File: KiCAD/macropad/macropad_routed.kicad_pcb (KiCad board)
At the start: 2 copper layers, 114.6 x 122.2 mm, 39 parts

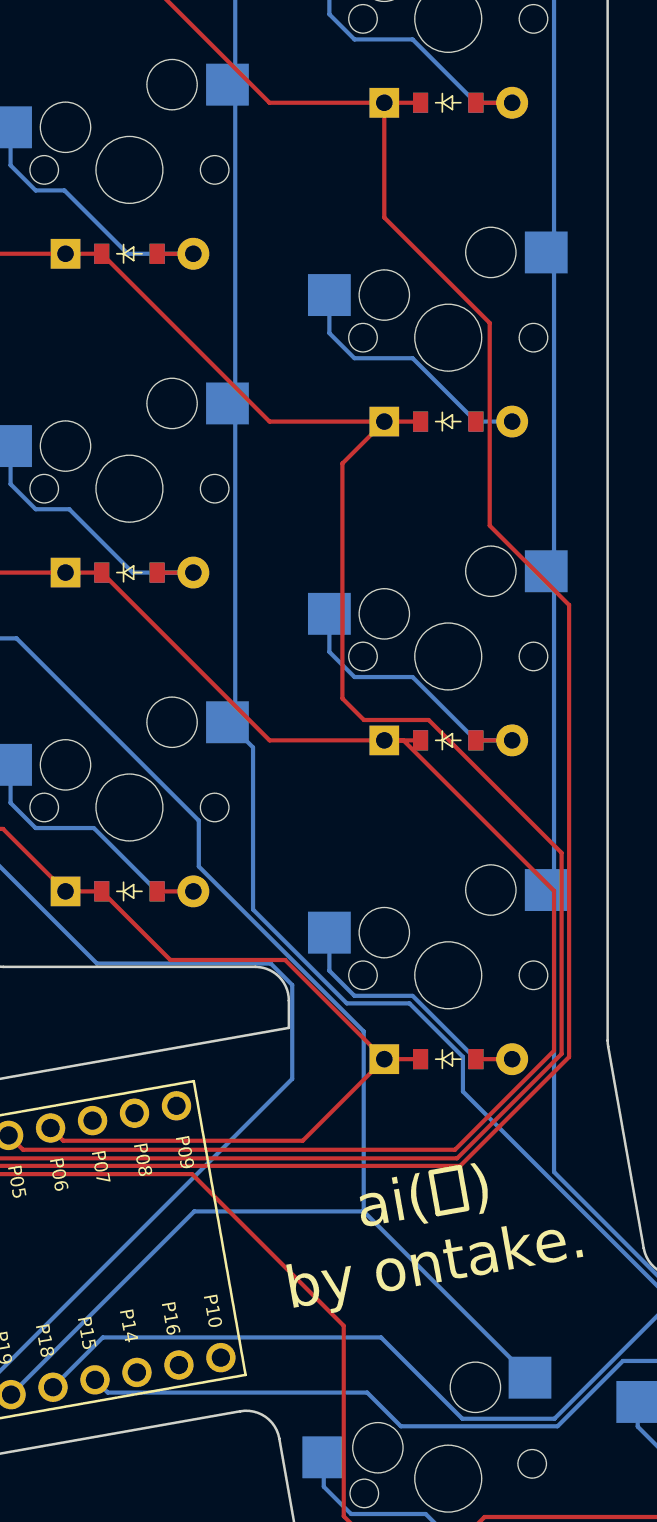
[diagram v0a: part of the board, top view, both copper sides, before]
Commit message: Fix probleme with rounding of the tracks
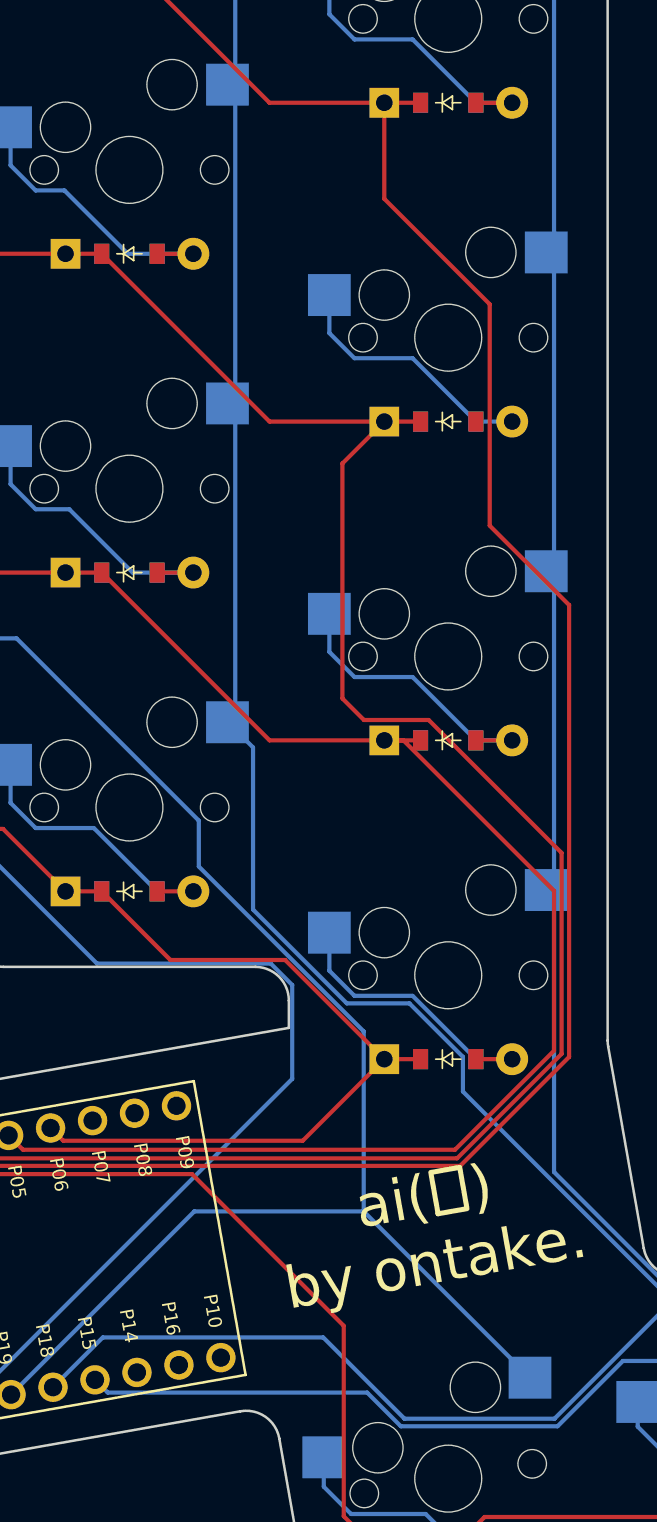
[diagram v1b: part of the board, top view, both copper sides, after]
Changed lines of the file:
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@@
   (segment (start 68.111731 76.886489) (end 64.05325 72.828008) (width 0.25) (layer "B.Cu") (net 8))
   (segment (start 64.05325 72.828008) (end 64.05325 70.56) (width 0.25) (layer "B.Cu") (net 8))
-  (segment (start 130.61 96.222296) (end 130.61 108.300776) (width 0.25) (layer "F.Cu") (net 9))
-  (segment (start 97.867567 146.45952) (end 96.934345 145.526298) (width 0.25) (layer "F.Cu") (net 9))
-  (segment (start 135.342711 139.968724) (end 128.851915 146.45952) (width 0.25) (layer "F.Cu") (net 9))
+  (segment (start 130.61 95.11) (end 130.61 108.300776) (width 0.25) (layer "F.Cu") (net 9))
   (segment (start 80.102829 74.325421) (end 86.32825 68.1) (width 0.25) (layer "F.Cu") (net 9))
   (segment (start 67.32825 78.1) (end 69.48825 78.1) (width 0.25) (layer "F.Cu") (net 9))
@@
   (segment (start 88.48825 68.1) (end 93.48825 73.1) (width 0.25) (layer "F.Cu") (net 9))
   (segment (start 86.32825 68.1) (end 88.48825 68.1) (width 0.25) (layer "F.Cu") (net 9))
-  (segment (start 135.342711 113.033487) (end 135.342711 139.968724) (width 0.25) (layer "F.Cu") (net 9))
   (segment (start 117.48825 83.1) (end 124.32825 83.1) (width 0.25) (layer "F.Cu") (net 9))
   (segment (start 124.32825 83.1) (end 126.48825 83.1) (width 0.25) (layer "F.Cu") (net 9))
   (segment (start 73.262829 74.325421) (end 80.102829 74.325421) (width 0.25) (layer "F.Cu") (net 9))
-  (segment (start 124.32825 89.940546) (end 130.61 96.222296) (width 0.25) (layer "F.Cu") (net 9))
+  (segment (start 135.342711 139.968724) (end 128.851915 146.45952) (width 0.25) (layer "F.Cu") (net 9))
+  (segment (start 97.867567 146.45952) (end 96.934345 145.526298) (width 0.25) (layer "F.Cu") (net 9))
   (segment (start 130.61 108.300776) (end 135.342711 113.033487) (width 0.25) (layer "F.Cu") (net 9))
+  (segment (start 135.342711 113.033487) (end 135.342711 139.968724) (width 0.25) (layer "F.Cu") (net 9))
+  (segment (start 128.851915 146.45952) (end 97.867567 146.45952) (width 0.25) (layer "F.Cu") (net 9))
+  (segment (start 124.32825 83.1) (end 124.32825 88.82825) (width 0.25) (layer "F.Cu") (net 9))
   (segment (start 105.32825 73.1) (end 107.48825 73.1) (width 0.25) (layer "F.Cu") (net 9))
-  (segment (start 124.32825 83.1) (end 124.32825 89.940546) (width 0.25) (layer "F.Cu") (net 9))
-  (segment (start 128.851915 146.45952) (end 97.867567 146.45952) (width 0.25) (layer "F.Cu") (net 9))
+  (segment (start 124.32825 88.82825) (end 130.61 95.11) (width 0.25) (layer "F.Cu") (net 9))
   (segment (start 91.78825 125.1) (end 93.94825 125.1) (width 0.25) (layer "F.Cu") (net 10))
   (segment (start 87.001505 121.325421) (end 84.550663 121.325421) (width 0.25) (layer "B.Cu") (net 10))
@@
   (segment (start 102.05325 124.828008) (end 102.05325 122.56) (width 0.25) (layer "B.Cu") (net 15))
   (segment (start 110.78825 130.1) (end 107.013671 126.325421) (width 0.25) (layer "B.Cu") (net 15))
+  (segment (start 125.530631 161.530631) (end 120.687559 156.687559) (width 0.25) (layer "B.Cu") (net 16))
   (segment (start 115.443671 101.483421) (end 115.443671 119.556579) (width 0.25) (layer "B.Cu") (net 16))
   (segment (start 129.013739 142.031367) (end 141.464646 154.482274) (width 0.25) (layer "B.Cu") (net 16))
   (segment (start 115.443671 81.556579) (end 114.98025 82.02) (width 0.25) (layer "B.Cu") (net 16))
   (segment (start 115.443671 82.483421) (end 115.443671 100.556579) (width 0.25) (layer "B.Cu") (net 16))
-  (segment (start 134.469369 161.530631) (end 128.981076 161.530631) (width 0.25) (layer "B.Cu") (net 16))
+  (segment (start 120.687559 156.687559) (end 107.548644 156.687559) (width 0.25) (layer "B.Cu") (net 16))
   (segment (start 141.464646 154.482274) (end 141.517726 154.482274) (width 0.25) (layer "B.Cu") (net 16))
+  (segment (start 134.469369 161.530631) (end 125.530631 161.530631) (width 0.25) (layer "B.Cu") (net 16))
   (segment (start 115.443671 100.556579) (end 114.98025 101.02) (width 0.25) (layer "B.Cu") (net 16))
   (segment (start 129.013739 139.961207) (end 129.013739 142.031367) (width 0.25) (layer "B.Cu") (net 16))
@@
   (segment (start 116.50525 131.186022) (end 122.094169 136.774941) (width 0.25) (layer "B.Cu") (net 16))
   (segment (start 115.00525 120.02) (end 116.50525 121.52) (width 0.25) (layer "B.Cu") (net 16))
-  (segment (start 128.981076 161.530631) (end 124.138004 156.687559) (width 0.25) (layer "B.Cu") (net 16))
   (segment (start 122.094169 136.774941) (end 125.827473 136.774941) (width 0.25) (layer "B.Cu") (net 16))
   (segment (start 114.98025 120.02) (end 115.00525 120.02) (width 0.25) (layer "B.Cu") (net 16))
+  (segment (start 107.548644 156.687559) (end 104.583567 159.652636) (width 0.25) (layer "B.Cu") (net 16))
   (segment (start 114.98025 63.02) (end 115.443671 63.483421) (width 0.25) (layer "B.Cu") (net 16))
   (segment (start 115.443671 119.556579) (end 114.98025 120.02) (width 0.25) (layer "B.Cu") (net 16))
   (segment (start 116.50525 121.52) (end 116.50525 131.186022) (width 0.25) (layer "B.Cu") (net 16))
   (segment (start 150.419576 154.482274) (end 151.720711 155.783409) (width 0.25) (layer "B.Cu") (net 16))
+  (segment (start 141.517726 154.482274) (end 134.469369 161.530631) (width 0.25) (layer "B.Cu") (net 16))
   (segment (start 114.98025 82.02) (end 115.443671 82.483421) (width 0.25) (layer "B.Cu") (net 16))
   (segment (start 115.443671 63.483421) (end 115.443671 81.556579) (width 0.25) (layer "B.Cu") (net 16))
   (segment (start 141.517726 154.482274) (end 150.419576 154.482274) (width 0.25) (layer "B.Cu") (net 16))
-  (segment (start 107.548644 156.687559) (end 104.583567 159.652636) (width 0.25) (layer "B.Cu") (net 16))
-  (segment (start 141.517726 154.482274) (end 134.469369 161.530631) (width 0.25) (layer "B.Cu") (net 16))
-  (segment (start 124.138004 156.687559) (end 107.548644 156.687559) (width 0.25) (layer "B.Cu") (net 16))
   (segment (start 110.78825 111.1) (end 112.94825 111.1) (width 0.25) (layer "F.Cu") (net 17))
   (segment (start 102.05325 105.828008) (end 102.05325 103.56) (width 0.25) (layer "B.Cu") (net 17))
